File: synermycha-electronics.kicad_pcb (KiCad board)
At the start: 4 copper layers, 50 x 75 mm, 151 parts, among them J1 BATT, J11 USB_B_Micro, J12 Conn_01x05, J13 Conn_01x05, J14 Conn_01x05, J15 Conn_01x05, J16 Conn_01x05, J17 Conn_01x03, J2 Conn_01x02, J3 Conn_01x02, J4 USB_B_Micro, J5 ESP_01, J6 A1250WV-S-4P, Q1 IRLML9301TRPBF, Q2 BC847, Q3 BC847, Q4 BC847, Q5 IRLML2060TRPBF, Q6 IRLML2060TRPBF, Q7 IRLML9301TRPBF, SW1 DTSM32N, SW2 DTSM32N, SW3 DTSM32N, SW4 DTSM32N, U1 LM1117LDX, U12 MPU-9250, U13 STM32F446RETx, U14 STM14_SW, U2 LM1117LDX, U3 LM1117LDX, U4 DRV8835, U5 LM1117LDX, U8 CP2102N-A01-GQFN28, U9 TS5A3167DBVR, Y1 16Mhz, 8pF

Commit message: QS
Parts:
- removed the REF** at (36.9, 168.5)
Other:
- outline, holes or cut-outs redrawn
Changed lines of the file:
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@@
-(kicad_pcb (version 20171130) (host pcbnew 5.1.5-52549c5~84~ubuntu18.04.1)
+(kicad_pcb (version 20171130) (host pcbnew "(5.1.5)-3")
   (general
     (thickness 1.6)
-    (drawings 49)
+    (drawings 35)
     (tracks 1610)
     (zones 0)
-    (modules 151)
+    (modules 150)
     (nets 105)
   )
@@
     (2 In2.Cu signal)
     (31 B.Cu signal)
-    (32 B.Adhes user hide)
-    (33 F.Adhes user hide)
-    (34 B.Paste user hide)
-    (35 F.Paste user hide)
+    (32 B.Adhes user)
+    (33 F.Adhes user)
+    (34 B.Paste user)
+    (35 F.Paste user)
     (36 B.SilkS user)
     (37 F.SilkS user)
@@
   )
   (setup
-    (last_trace_width 0.3048)
+    (last_trace_width 0.25)
     (user_trace_width 0.1524)
     (user_trace_width 0.2032)
@@
     (pad "" np_thru_hole circle (at 0 0) (size 0.8 0.8) (drill 0.762) (layers *.Cu *.Mask))
   )
-  (module mocowanie_silników:mocowanie_silników (layer F.Cu)
-    (at 36.9 168.5 180)
-    (fp_text reference REF** (at 16 5.75) (layer F.SilkS) hide
-      (effects (font (size 1 1) (thickness 0.15)))
-    )
-    (fp_text value mocowanie_silników (at 16 4.75) (layer F.Fab)
-      (effects (font (size 1 1) (thickness 0.15)))
-    )
-    (fp_line (start 0 9) (end 1 8) (layer Dwgs.User) (width 0.12))
-    (fp_line (start -1 8) (end 0 9) (layer Dwgs.User) (width 0.12))
-    (fp_line (start 0 9) (end -1 8) (layer Dwgs.User) (width 0.12))
-    (fp_line (start 0 4) (end 0 9) (layer Dwgs.User) (width 0.12))
-    (fp_line (start 0 9) (end 0 4) (layer Dwgs.User) (width 0.12))
-    (fp_circle (center 10.75 10.75) (end 10.75 11.75) (layer Dwgs.User) (width 0.12))
-    (fp_circle (center -11 10.75) (end -11 11.75) (layer Dwgs.User) (width 0.12))
-    (fp_circle (center 10.75 -12.75) (end 10.5 -13.75) (layer Dwgs.User) (width 0.12))
-    (fp_circle (center -11 -12.75) (end -10.75 -13.75) (layer Dwgs.User) (width 0.12))
-    (fp_line (start -11 10.75) (end -11 -12.75) (layer Dwgs.User) (width 0.12))
-    (fp_line (start 10.75 10.75) (end -11 10.75) (layer Dwgs.User) (width 0.12))
-    (fp_line (start 10.75 -12.75) (end 10.75 10.75) (layer Dwgs.User) (width 0.12))
-    (fp_line (start -11 -12.75) (end 10.75 -12.75) (layer Dwgs.User) (width 0.12))
-    (model ${KIPRJMOD}/3D_models/mocowanie-napędów.stp
-      (offset (xyz -0.12 1 14.5))
-      (scale (xyz 1 1 1))
-      (rotate (xyz 90 0 0))
-    )
-  )
   (module graphics:SynerMycha_napis_silk_screen_45.1x17mm locked (layer B.Cu)
     (at 37 166 90)
@@
     )
   )
-  (gr_arc (start 52.5 161.5) (end 52.5 161) (angle -90) (layer Edge.Cuts) (width 0.05))
-  (gr_arc (start 52.5 177.5) (end 52 177.5) (angle -90) (layer Edge.Cuts) (width 0.05))
-  (gr_arc (start 21.5 177.5) (end 21.5 178) (angle -90) (layer Edge.Cuts) (width 0.05))
-  (gr_arc (start 21.5 161.5) (end 22 161.5) (angle -90) (layer Edge.Cuts) (width 0.05))
-  (gr_arc (start 59.95 138.85) (end 62 138.85) (angle -45.04113441) (layer Edge.Cuts) (width 0.05))
-  (gr_arc (start 46.15 125.05) (end 47.599998 123.6) (angle -44.95879138) (layer Edge.Cuts) (width 0.05))
-  (gr_arc (start 27.85 125.05) (end 27.85 123) (angle -45.04113441) (layer Edge.Cuts) (width 0.05))
-  (gr_arc (start 14.05 138.85) (end 12.6 137.400002) (angle -44.95879138) (layer Edge.Cuts) (width 0.05))
-  (gr_arc (start 13 160) (end 12 160) (angle -90) (layer Edge.Cuts) (width 0.05))
-  (gr_arc (start 61 160) (end 61 161) (angle -90) (layer Edge.Cuts) (width 0.05))
-  (gr_arc (start 61 179) (end 62 179) (angle -90) (layer Edge.Cuts) (width 0.05))
-  (gr_arc (start 13 179) (end 13 178) (angle -90) (layer Edge.Cuts) (width 0.05))
-  (gr_arc (start 13 197) (end 12 197) (angle -90) (layer Edge.Cuts) (width 0.05))
-  (gr_arc (start 61 197) (end 61 198) (angle -90) (layer Edge.Cuts) (width 0.05))
   (dimension 17 (width 0.15) (layer Dwgs.User)
     (gr_text "17,000 mm" (at -11.3 169.5 90) (layer Dwgs.User)
@@
   )
   (gr_line (start 52.5 178) (end 52.5 178) (layer Edge.Cuts) (width 0.05))
-  (gr_line (start 12 179) (end 12 183) (layer Edge.Cuts) (width 0.05))
-  (gr_line (start 21.5 178) (end 13 178) (layer Edge.Cuts) (width 0.05))
-  (gr_line (start 62 179) (end 62 183) (layer Edge.Cuts) (width 0.05))
-  (gr_line (start 52.5 178) (end 61 178) (layer Edge.Cuts) (width 0.05))
-  (gr_line (start 62 160) (end 62 158) (layer Edge.Cuts) (width 0.05))
-  (gr_line (start 52.5 161) (end 61 161) (layer Edge.Cuts) (width 0.05))
-  (gr_line (start 12 158) (end 12 160) (layer Edge.Cuts) (width 0.05))
-  (gr_line (start 47.599998 123.6) (end 61.4 137.4) (layer Edge.Cuts) (width 0.05))
+  (gr_line (start 12 178) (end 12 183) (layer Edge.Cuts) (width 0.05))
+  (gr_line (start 22 178) (end 12 178) (layer Edge.Cuts) (width 0.05))
+  (gr_line (start 62 178) (end 62 183) (layer Edge.Cuts) (width 0.05))
+  (gr_line (start 52 178) (end 62 178) (layer Edge.Cuts) (width 0.05))
+  (gr_line (start 62 161) (end 62 158) (layer Edge.Cuts) (width 0.05))
+  (gr_line (start 52 161) (end 62 161) (layer Edge.Cuts) (width 0.05))
+  (gr_line (start 12 158) (end 12 161) (layer Edge.Cuts) (width 0.05))
+  (gr_line (start 47 123) (end 62 138) (layer Edge.Cuts) (width 0.05))
   (gr_text ↑ (at 51.25 191) (layer F.SilkS)
     (effects (font (size 2 1.5) (thickness 0.2)))
@@
     (effects (font (size 1 1) (thickness 0.15)))
   )
-  (gr_line (start 62 183) (end 62 197) (layer Edge.Cuts) (width 0.05))
-  (gr_line (start 52 161.5) (end 52 177.5) (layer Edge.Cuts) (width 0.05))
-  (gr_line (start 62 138.85) (end 62 158) (layer Edge.Cuts) (width 0.05))
-  (gr_line (start 12 158) (end 11.999392 138.848527) (layer Edge.Cuts) (width 0.05))
-  (gr_line (start 21.5 161) (end 13 161) (layer Edge.Cuts) (width 0.05))
-  (gr_line (start 22 177.5) (end 22 161.5) (layer Edge.Cuts) (width 0.05))
-  (gr_line (start 12 197) (end 12 183) (layer Edge.Cuts) (width 0.05))
+  (gr_line (start 62 183) (end 62 198) (layer Edge.Cuts) (width 0.05))
+  (gr_line (start 52 161) (end 52 178) (layer Edge.Cuts) (width 0.05))
+  (gr_line (start 62 138) (end 62 158) (layer Edge.Cuts) (width 0.05))
+  (gr_line (start 12 158) (end 12 138) (layer Edge.Cuts) (width 0.05))
+  (gr_line (start 22 161) (end 12 161) (layer Edge.Cuts) (width 0.05))
+  (gr_line (start 22 178) (end 22 161) (layer Edge.Cuts) (width 0.05))
+  (gr_line (start 12 198) (end 12 183) (layer Edge.Cuts) (width 0.05))
   (gr_text ↑ (at 51.25 196.5 180) (layer F.SilkS)
     (effects (font (size 2 1.5) (thickness 0.2)))
@@
     (arrow2b (pts (xy -10 123) (xy -9.413579 124.126504)))
   )
-  (gr_line (start 61 198) (end 13 198) (layer Edge.Cuts) (width 0.05))
-  (gr_line (start 27.85 123) (end 46.15 123) (layer Edge.Cuts) (width 0.05))
-  (gr_line (start 12.6 137.400002) (end 26.4 123.6) (layer Edge.Cuts) (width 0.05))
+  (gr_line (start 62 198) (end 12 198) (layer Edge.Cuts) (width 0.05))
+  (gr_line (start 27 123) (end 47 123) (layer Edge.Cuts) (width 0.05))
+  (gr_line (start 12 138) (end 27 123) (layer Edge.Cuts) (width 0.05))
   (via (at 49.6 169.1) (size 0.6) (drill 0.3) (layers F.Cu B.Cu) (net 1))
   (via (at 44 151.7) (size 0.6) (drill 0.3) (layers F.Cu B.Cu) (net 1))

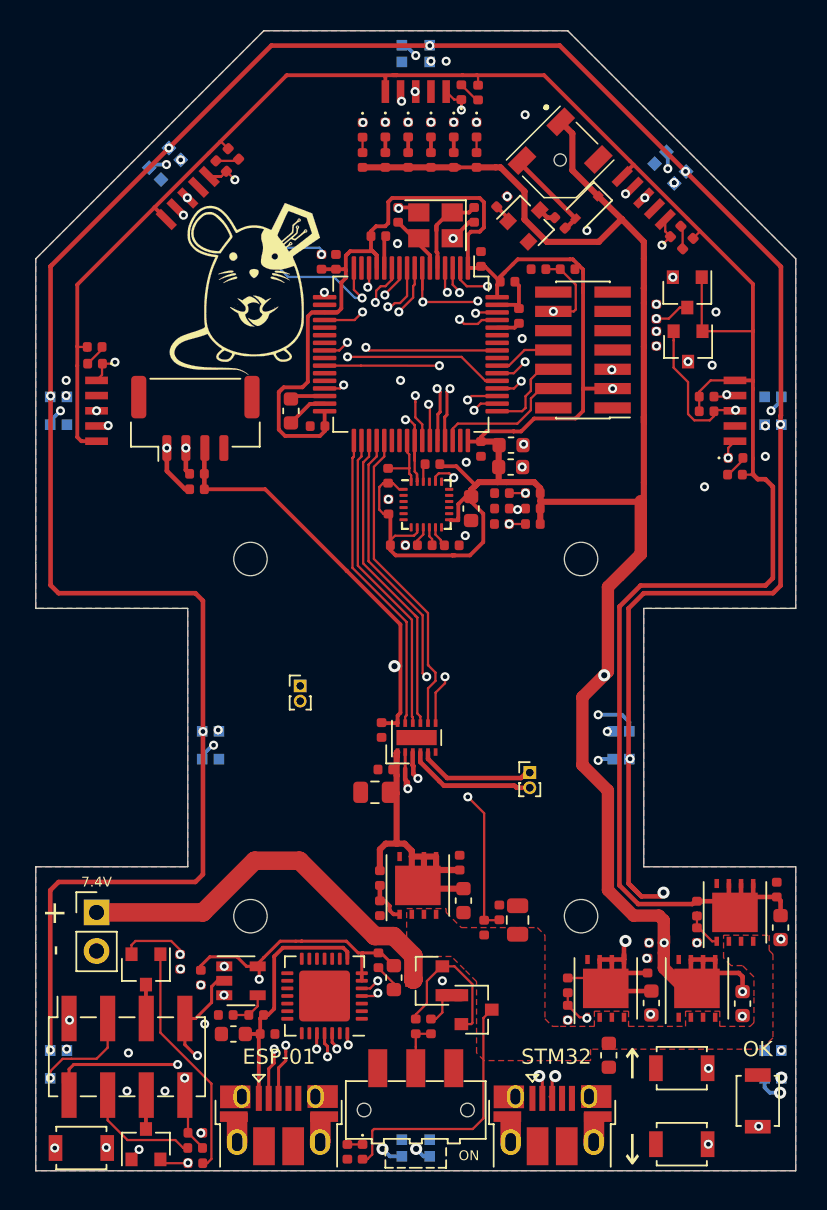
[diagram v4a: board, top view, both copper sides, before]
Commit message: Finished encoders, added XSHUT pullups
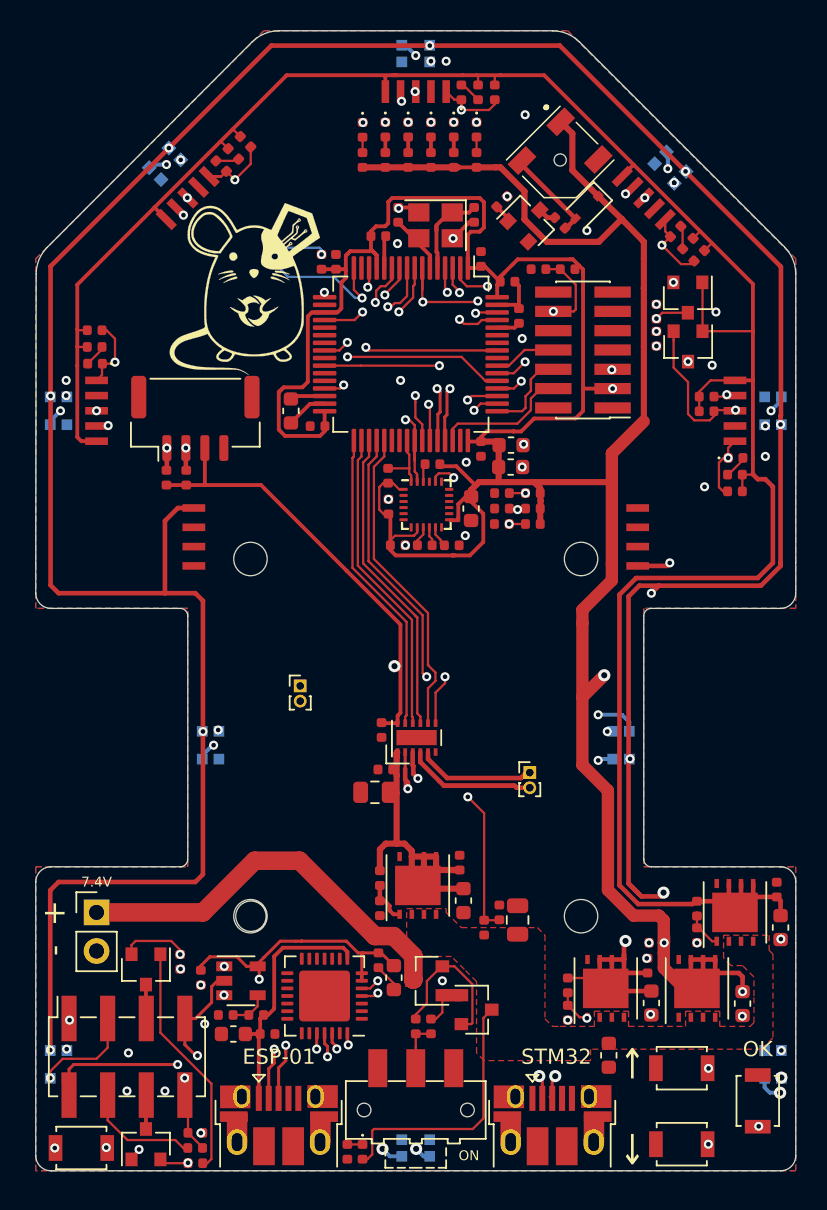
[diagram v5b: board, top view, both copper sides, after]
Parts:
- removed the REF** at (27.8, 137.8)
- added J7: Conn_01x04, connector_brd2brd:01x04_1.0x0.5mm_SMD, F.Cu at (22.4, 156.3)
- added J8: Conn_01x04, connector_brd2brd:01x04_1.0x0.5mm_SMD, F.Cu at (51.6, 156.3)
- added R36: 2K7, Resistor_SMD:R_0402_1005Metric, F.Cu at (55.6, 137.8)
- added R37: 2K7, Resistor_SMD:R_0402_1005Metric, F.Cu at (58.0, 153.3)
- added R38: 2K7, Resistor_SMD:R_0402_1005Metric, F.Cu at (15.9, 142.7)
- added R39: 2K7, Resistor_SMD:R_0402_1005Metric, F.Cu at (42.2, 127.0)
- added R40: 2K7, Resistor_SMD:R_0402_1005Metric, F.Cu at (25.8, 130.3)
- added REF**: mocowanie_silników, mocowanie_silników:mocowanie_silników, F.Cu at (36.9, 168.5)
- C30, C31: value 8pF -> 18pF
- Y1: value 16Mhz, 8pF -> 16Mhz, 18pF
- moved R11 2.15 mm to (20.6, 152.4), turned to 90 degrees
- moved R30 0.75 mm to (21.9, 152.4), turned to 90 degrees
- moved Q5 0.34 mm to (54.9, 140.6)
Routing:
- net +5V: track 258.2 -> 270.3 mm, vias 12 -> 14
- net +3V3: track 338.5 -> 332.7 mm
- net +2V8: track 155.3 -> 158.6 mm
- net /Distance Sensors/VL53L0x_~XSHUT[2]: track 20.6 -> 23.7 mm
- net /Distance Sensors/VL53L0x_~XSHUT[5]: track 17.4 -> 20.1 mm
- net /Distance Sensors/VL53L0x_~XSHUT[1]: track 18.3 -> 20.9 mm
- net /Distance Sensors/VL53L0x_~XSHUT[3]: track 20.1 -> 22.7 mm
- net /Distance Sensors/VL53L0x_~XSHUT[4]: track 22.4 -> 25.0 mm
- net /LED & Oled & Buzzer/LCD_SDA: track 28.9 -> 26.9 mm
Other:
- outline, holes or cut-outs redrawn

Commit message: Changed location of battery connector
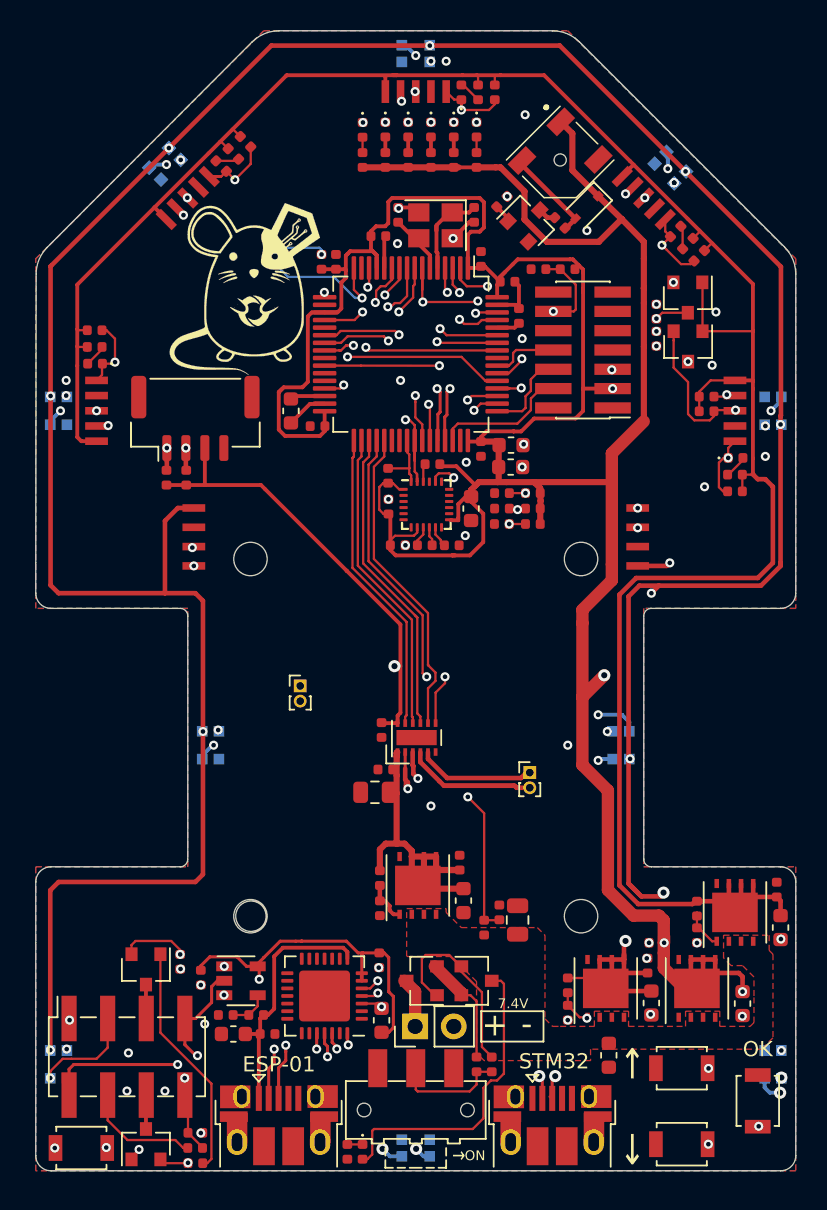
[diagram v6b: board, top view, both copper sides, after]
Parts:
- moved J1 22.3 mm to (37.0, 188.5), turned to 90 degrees
- moved R51 4.72 mm to (41.0, 191.0)
- moved R52 4.72 mm to (42.0, 191.0)
- moved C16 2.92 mm to (34.8, 188.1), turned to 90 degrees
- moved Q7 1.90 mm to (41.0, 185.5)
- moved Q1 0.35 mm to (37.4, 185.5)
- moved C17 0.06 mm to (34.6, 184.2)
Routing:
- net /Encoders/ENC_L_B: track 0.00 -> 26.6 mm, vias 0 -> 2
- net /Encoders/ENC_L_A: track 0.00 -> 24.1 mm, vias 0 -> 2
- net /Encoders/ENC_R_A: track 0.00 -> 23.7 mm, vias 0 -> 2
- net /Power Section/BATT+: track 26.4 -> 3.29 mm
- net /Encoders/ENC_R_B: track 0.00 -> 22.8 mm, vias 0 -> 2
- net Net-(Q1-Pad1): track 3.31 -> 12.6 mm
- net +3V3: track 332.7 -> 337.8 mm
- net Net-(J17-Pad2): track 3.26 -> 7.48 mm
- net /Power Section/VCC: track 17.4 -> 20.5 mm
- net Net-(Q1-Pad2): track 9.99 -> 7.46 mm
- net /Buttons/~BUTTON_DOWN: track 70.5 -> 69.8 mm
- net /Distance Sensors/VL53L0x_~XSHUT[3]: track 22.7 -> 23.3 mm
- net GND: track 16.7 -> 16.2 mm, vias 38 -> 41

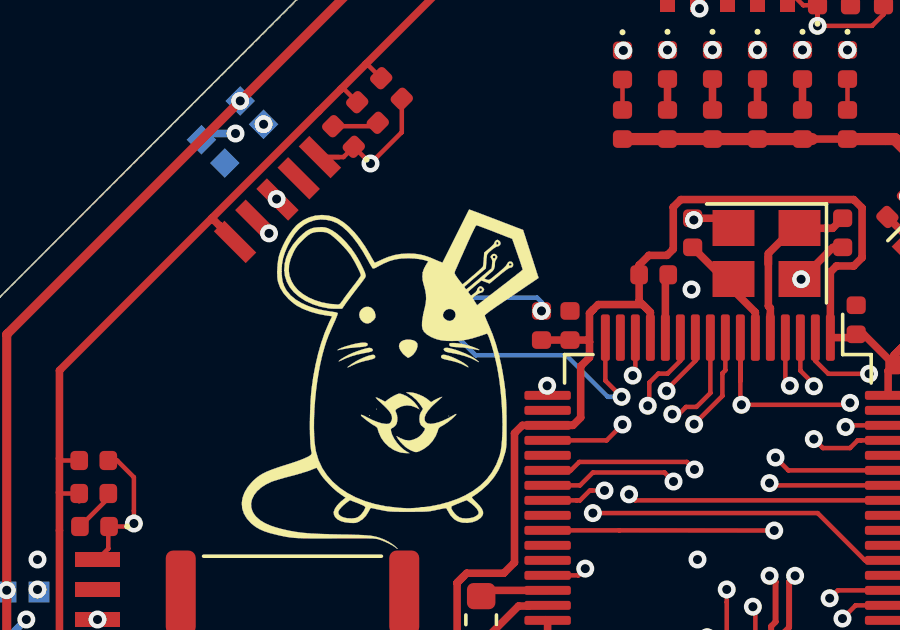
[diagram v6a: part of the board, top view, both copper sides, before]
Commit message: Flip led, fix path
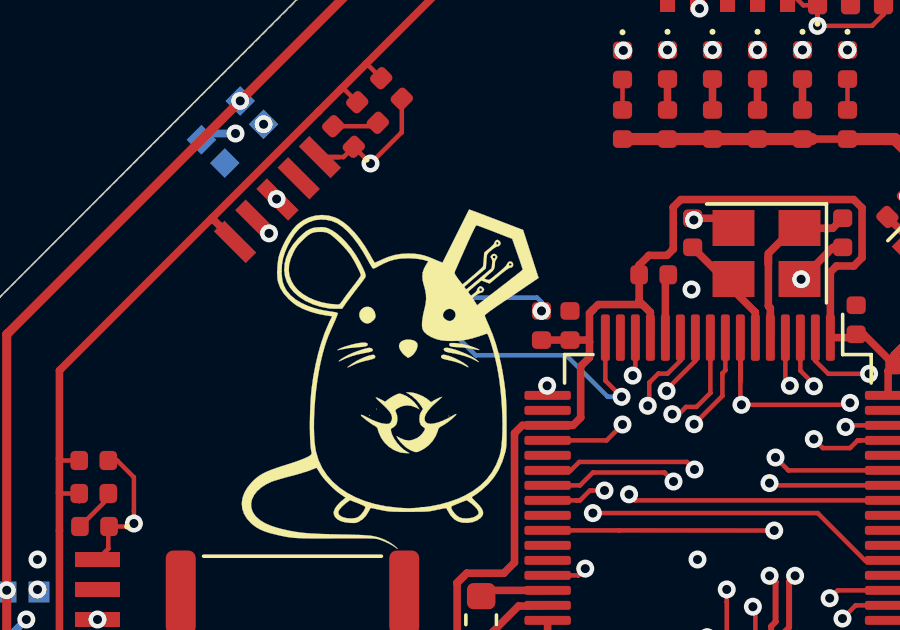
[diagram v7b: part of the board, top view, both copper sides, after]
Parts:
- added REF**: hole_0.8mm, holes:hole_0.8mm, F.Cu at (27.8, 137.8)
- turned D23 to 90 degrees
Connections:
- D23 pad 1: Net-(D23-Pad1) -> /LED & Oled & Buzzer/~LED_MOUSE_EYE
- D23 pad 2: /LED & Oled & Buzzer/~LED_MOUSE_EYE -> Net-(D23-Pad2)
- R27 pad 1: Net-(D23-Pad1) -> Net-(D23-Pad2)
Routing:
- net Net-(D23-Pad2): track 0.00 -> 3.41 mm, vias 0 -> 1
- net Net-(D23-Pad1): track 3.41 -> 0.00 mm, vias 1 -> 0

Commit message: Cosmetics
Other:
- board text added: "v1.0 s.mroz, b.ostr, s.dac @PWr 2020"
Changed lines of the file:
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@@
   (general
     (thickness 1.6)
-    (drawings 54)
+    (drawings 55)
     (tracks 1727)
     (zones 0)
@@
     )
   )
+  (gr_text "v1.0\ns.mroz, b.ostr, \ns.dac\n@PWr 2020" (at 13.5 181) (layer F.SilkS)
+    (effects (font (size 0.7 0.7) (thickness 0.1)) (justify left))
+  )
   (gr_text ↑ (at 39.8 197 270) (layer F.SilkS)
